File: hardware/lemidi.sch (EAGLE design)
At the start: 67 parts, among them Q1 IRLML6246, Q2 IRLML6246, Q3 IRLML6246, Q4 IRLML6246, U1 SPX5205 3v3, X3 debug, Y2 12MHz 0.25%, Y3 8MHz

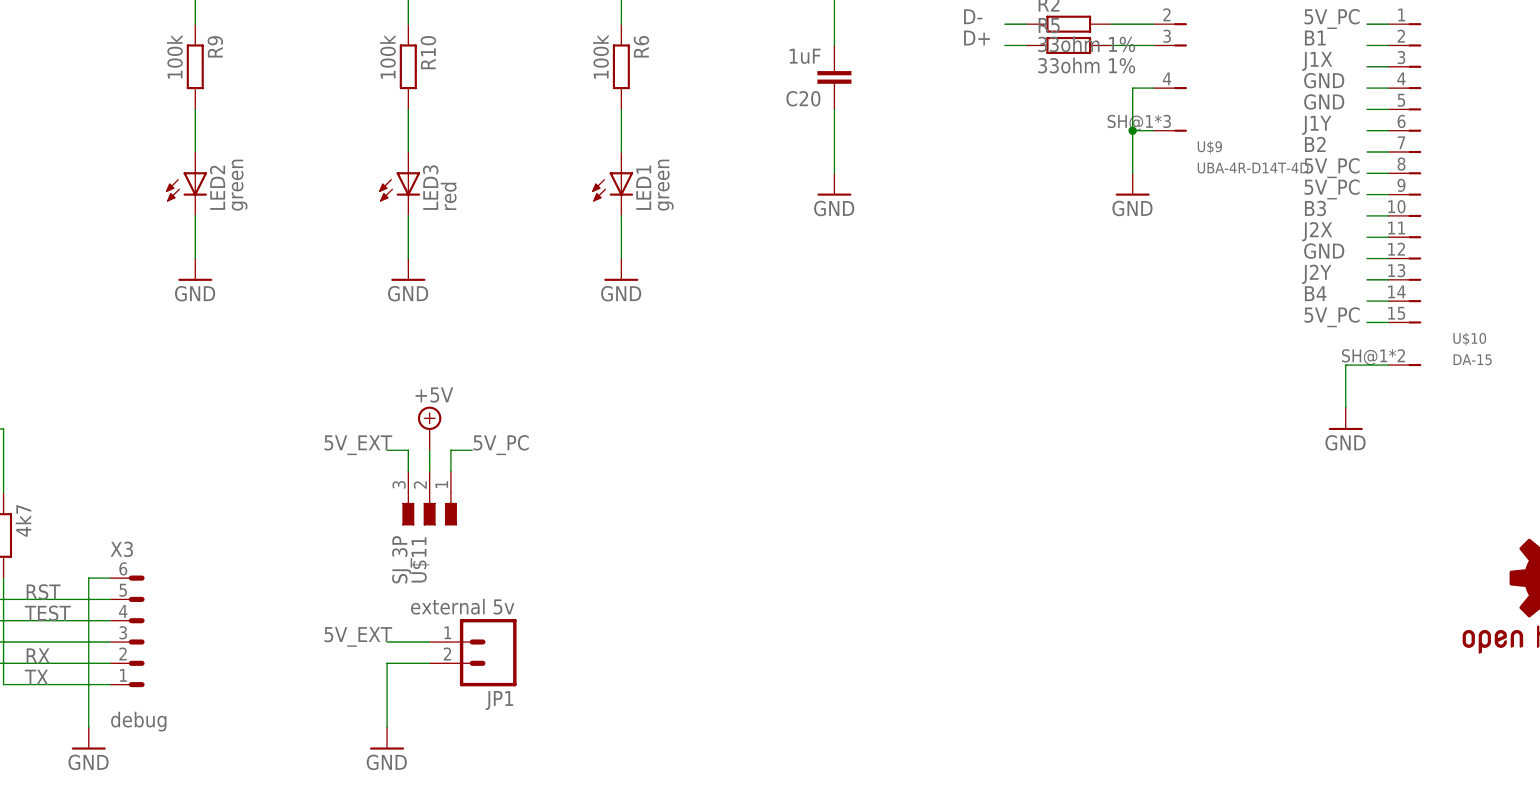
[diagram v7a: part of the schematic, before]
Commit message: split 5v inputs from the midi connector, add fuse, add reverse polarity protection for external 5v input
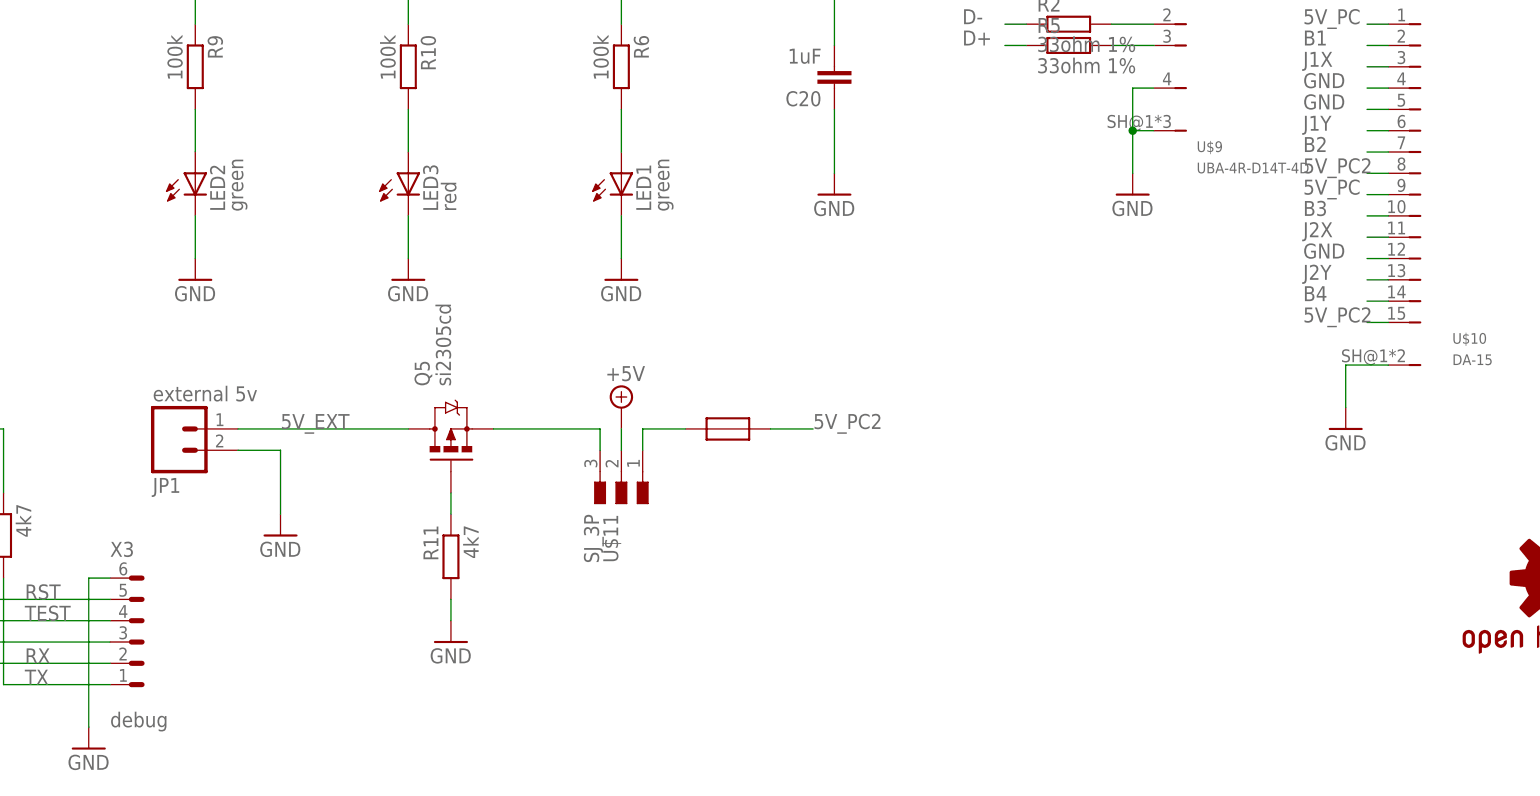
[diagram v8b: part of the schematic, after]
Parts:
- added Q5: si2305cd, Simplex-DiscreteSemi:MOSFET-PCHANNELSMD_POWER
- added R11: 4k7, rcl:R-EU_R0805W
- added U$12: RESETTABLE_1210, Simplex-Fuses:RESETTABLE_1210
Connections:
- new net 5V_PC2: U$10.15, U$10.8, U$12.P$2
- new net N$10: U$11.1, U$12.P$1
- new net N$23: Q5.S, U$11.3
- new net N$24: Q5.G, R11.1
- net 5V_EXT: now also Q5.D; no longer U$11.3
- net 5V_PC: no longer U$10.15, U$10.8, U$11.1
- net GND: now also R11.2
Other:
- moved on the sheet: JP1, U$11
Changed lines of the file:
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@@
 <part name="TP5" library="testpad" deviceset="TP" device="TP12R" value=""/>
 <part name="JP1" library="SparkFun-Connectors" deviceset="M02" device="PTH" value="external 5v"/>
+<part name="U$12" library="Simplex-Fuses" deviceset="RESETTABLE" device="_1210"/>
+<part name="Q5" library="Simplex-DiscreteSemi" deviceset="MOSFET-PCHANNEL" device="SMD_POWER" value="si2305cd"/>
+<part name="R11" library="rcl" deviceset="R-EU_" device="R0805W" value="4k7"/>
+<part name="GND47" library="SparkFun" deviceset="GND" device=""/>
 </parts>
 <sheets>
@@
 <instance part="GND10" gate="1" x="40.64" y="58.42"/>
 <instance part="U$2" gate="G$1" x="96.52" y="27.94" rot="R180"/>
-<instance part="GND15" gate="1" x="304.8" y="7.62"/>
+<instance part="GND15" gate="1" x="292.1" y="33.02"/>
 <instance part="R6" gate="G$1" x="332.74" y="88.9" rot="R270"/>
 <instance part="GND36" gate="1" x="332.74" y="63.5"/>
@@
 <instance part="C13" gate="G$1" x="200.66" y="132.08" rot="R180"/>
 <instance part="GND29" gate="1" x="200.66" y="124.46"/>
-<instance part="U$11" gate="G$1" x="309.88" y="35.56" rot="R270"/>
-<instance part="SUPPLY9" gate="+5V" x="309.88" y="45.72"/>
+<instance part="U$11" gate="G$1" x="332.74" y="38.1" rot="R270"/>
+<instance part="SUPPLY9" gate="+5V" x="332.74" y="48.26"/>
 <instance part="C14" gate="G$1" x="243.84" y="15.24" rot="R180"/>
 <instance part="GND31" gate="1" x="243.84" y="7.62"/>
@@
 <instance part="GND46" gate="1" x="187.96" y="12.7"/>
 <instance part="TP5" gate="G$1" x="167.64" y="45.72" rot="R270"/>
-<instance part="JP1" gate="G$1" x="317.5" y="20.32" rot="R180"/>
+<instance part="JP1" gate="G$1" x="279.4" y="45.72" rot="MR180"/>
+<instance part="U$12" gate="G$1" x="345.44" y="45.72"/>
+<instance part="Q5" gate="G$1" x="312.42" y="45.72" rot="R90"/>
+<instance part="R11" gate="G$1" x="312.42" y="30.48" rot="MR270"/>
+<instance part="GND47" gate="1" x="312.42" y="20.32"/>
 </instances>
 <busses>
@@
 <segment>
 <pinref part="GND15" gate="1" pin="GND"/>
-<wire x1="304.8" y1="17.78" x2="304.8" y2="10.16" width="0.1524" layer="91"/>
-<wire x1="304.8" y1="17.78" x2="309.88" y2="17.78" width="0.1524" layer="91"/>
+<wire x1="292.1" y1="43.18" x2="292.1" y2="35.56" width="0.1524" layer="91"/>
+<wire x1="292.1" y1="43.18" x2="287.02" y2="43.18" width="0.1524" layer="91"/>
 <pinref part="JP1" gate="G$1" pin="2"/>
 </segment>
@@
 <wire x1="101.6" y1="144.78" x2="116.84" y2="144.78" width="0.1524" layer="91"/>
 <wire x1="116.84" y1="144.78" x2="116.84" y2="139.7" width="0.1524" layer="91"/>
+</segment>
+<segment>
+<pinref part="R11" gate="G$1" pin="2"/>
+<pinref part="GND47" gate="1" pin="GND"/>
+<wire x1="312.42" y1="25.4" x2="312.42" y2="22.86" width="0.1524" layer="91"/>
 </segment>
 </net>
@@
 </segment>
 <segment>
-<pinref part="U$10" gate="G$1" pin="8"/>
-<wire x1="424.18" y1="76.2" x2="421.64" y2="76.2" width="0.1524" layer="91"/>
-<label x="414.02" y="76.2" size="1.778" layer="95"/>
-</segment>
-<segment>
 <pinref part="U$10" gate="G$1" pin="9"/>
 <wire x1="424.18" y1="73.66" x2="421.64" y2="73.66" width="0.1524" layer="91"/>
@@
 </segment>
 <segment>
-<pinref part="U$10" gate="G$1" pin="15"/>
-<wire x1="424.18" y1="58.42" x2="421.64" y2="58.42" width="0.1524" layer="91"/>
-<label x="414.02" y="58.42" size="1.778" layer="95"/>
-</segment>
-<segment>
 <pinref part="U$4" gate="G$1" pin="HA"/>
 <wire x1="284.48" y1="205.74" x2="287.02" y2="205.74" width="0.1524" layer="91"/>
@@
 <wire x1="284.48" y1="144.78" x2="287.02" y2="144.78" width="0.1524" layer="91"/>
 <label x="287.02" y="144.78" size="1.778" layer="95"/>
-</segment>
-<segment>
-<pinref part="U$11" gate="G$1" pin="1"/>
-<wire x1="312.42" y1="40.64" x2="312.42" y2="43.18" width="0.1524" layer="91"/>
-<wire x1="312.42" y1="43.18" x2="314.96" y2="43.18" width="0.1524" layer="91"/>
-<label x="314.96" y="43.18" size="1.778" layer="95"/>
 </segment>
 </net>
@@
 <pinref part="U$11" gate="G$1" pin="2"/>
 <pinref part="SUPPLY9" gate="+5V" pin="+5V"/>
-<wire x1="309.88" y1="40.64" x2="309.88" y2="43.18" width="0.1524" layer="91"/>
+<wire x1="332.74" y1="43.18" x2="332.74" y2="45.72" width="0.1524" layer="91"/>
 </segment>
 <segment>
@@
 <net name="5V_EXT" class="0">
 <segment>
-<wire x1="309.88" y1="20.32" x2="304.8" y2="20.32" width="0.1524" layer="91"/>
-<label x="297.18" y="20.32" size="1.778" layer="95"/>
+<label x="292.1" y="45.72" size="1.778" layer="95"/>
 <pinref part="JP1" gate="G$1" pin="1"/>
-</segment>
-<segment>
-<pinref part="U$11" gate="G$1" pin="3"/>
-<wire x1="307.34" y1="40.64" x2="307.34" y2="43.18" width="0.1524" layer="91"/>
-<wire x1="307.34" y1="43.18" x2="304.8" y2="43.18" width="0.1524" layer="91"/>
-<label x="297.18" y="43.18" size="1.778" layer="95"/>
+<wire x1="287.02" y1="45.72" x2="307.34" y2="45.72" width="0.1524" layer="91"/>
+<pinref part="Q5" gate="G$1" pin="D"/>
 </segment>
 </net>
@@
 </segment>
 </net>
+<net name="5V_PC2" class="0">
+<segment>
+<pinref part="U$10" gate="G$1" pin="8"/>
+<wire x1="424.18" y1="76.2" x2="421.64" y2="76.2" width="0.1524" layer="91"/>
+<label x="414.02" y="76.2" size="1.778" layer="95"/>
+</segment>
+<segment>
+<pinref part="U$10" gate="G$1" pin="15"/>
+<wire x1="424.18" y1="58.42" x2="421.64" y2="58.42" width="0.1524" layer="91"/>
+<label x="414.02" y="58.42" size="1.778" layer="95"/>
+</segment>
+<segment>
+<wire x1="350.52" y1="45.72" x2="355.6" y2="45.72" width="0.1524" layer="91"/>
+<label x="355.6" y="45.72" size="1.778" layer="95"/>
+<pinref part="U$12" gate="G$1" pin="P$2"/>
+</segment>
+</net>
+<net name="N$10" class="0">
+<segment>
+<pinref part="U$11" gate="G$1" pin="1"/>
+<wire x1="335.28" y1="43.18" x2="335.28" y2="45.72" width="0.1524" layer="91"/>
+<wire x1="335.28" y1="45.72" x2="340.36" y2="45.72" width="0.1524" layer="91"/>
+<pinref part="U$12" gate="G$1" pin="P$1"/>
+</segment>
+</net>
+<net name="N$23" class="0">
+<segment>
+<pinref part="Q5" gate="G$1" pin="S"/>
+<pinref part="U$11" gate="G$1" pin="3"/>
+<wire x1="317.5" y1="45.72" x2="330.2" y2="45.72" width="0.1524" layer="91"/>
+<wire x1="330.2" y1="45.72" x2="330.2" y2="43.18" width="0.1524" layer="91"/>
+</segment>
+</net>
+<net name="N$24" class="0">
+<segment>
+<pinref part="Q5" gate="G$1" pin="G"/>
+<pinref part="R11" gate="G$1" pin="1"/>
+<wire x1="312.42" y1="38.1" x2="312.42" y2="35.56" width="0.1524" layer="91"/>
+</segment>
+</net>
